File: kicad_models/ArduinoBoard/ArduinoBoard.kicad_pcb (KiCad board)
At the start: 2 copper layers, 90.5 x 70 mm, 21 parts, among them J1 5V Output, J2 Buttons, J3 PWM Output, J4 12V Input, J5 Conn_01x04_Pin, J6 Conn_01x04_Pin, J7 Conn_01x06_Pin, J8 Conn_01x06_Pin, J9 Position Input, SW1 SW_Push_Dual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

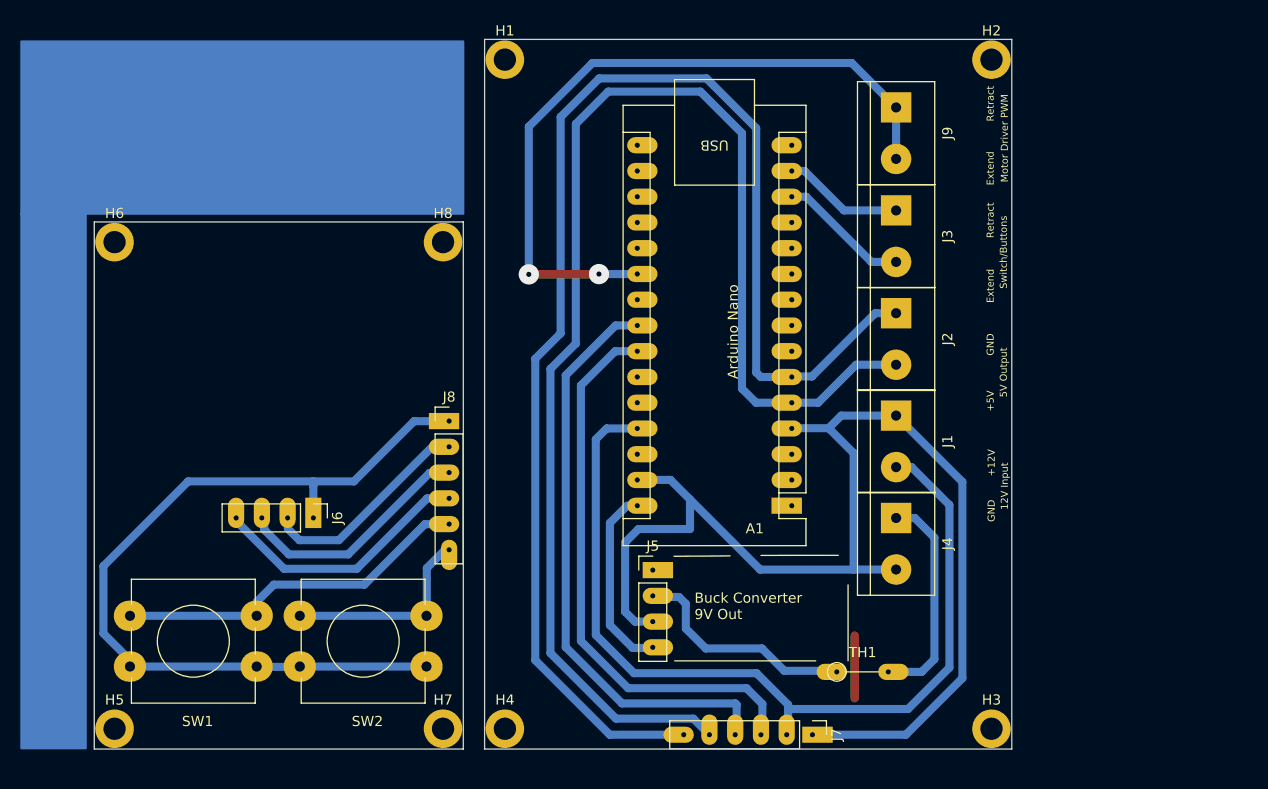
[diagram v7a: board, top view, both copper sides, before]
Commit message: Made some pretty significant changes to the PCB layout. Removed the need for a via path to cross over a couple of tracks.
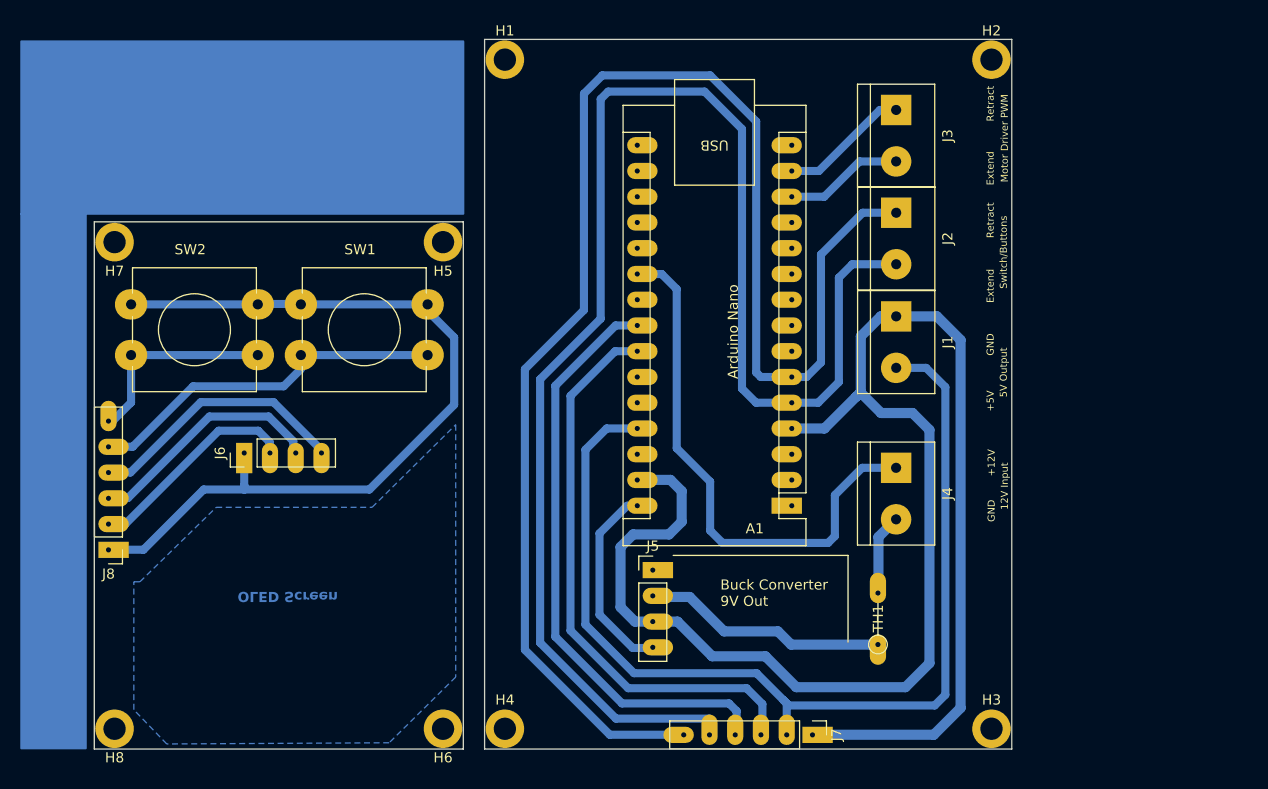
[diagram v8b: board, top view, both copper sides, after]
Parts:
- removed J9: Position Input, TerminalBlock:TerminalBlock_bornier-2_P5.08mm
- moved H5 57.9 mm to (84.4, 70.5), turned to 180 degrees
- moved H6 57.9 mm to (84.4, 118.5), turned to 180 degrees
- moved H7 57.9 mm to (52.0, 70.5), turned to 180 degrees
- moved H8 57.9 mm to (52.0, 118.5), turned to 180 degrees
- moved SW2 46.1 mm to (53.6, 76.6), turned to 0 degrees
- moved SW1 36.0 mm to (70.4, 76.6), turned to 0 degrees
- moved J8 35.9 mm to (51.4, 100.8), turned to 180 degrees
- moved J2 9.91 mm to (129.1, 67.6)
- moved J3 9.91 mm to (129.1, 57.5)
- moved J1 9.79 mm to (129.1, 77.8)
- moved J6 9.36 mm to (64.8, 91.3), turned to 90 degrees
- moved J4 4.95 mm to (129.1, 92.8)
- moved TH1 4.88 mm to (127.3, 110.2), turned to 90 degrees
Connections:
- net Net-(A1-VIN) renamed /VO+
- net Net-(J5-Pin_2) renamed /VI+
- net Net-(J6-Pin_1) renamed OLED_Board_GND
- net Net-(J6-Pin_2) renamed OLED_Board_5V
- net Net-(J8-Pin_6) renamed OLED_Board_Extend_Button
- A1 pad 29: Net-(J1-Pin_1) -> /GND
- A1 pad 4: Net-(J1-Pin_1) -> /GND
- J1 pad 1: Net-(J1-Pin_1) -> /GND
- J4 pad 1: Net-(J4-Pin_1) -> Net-(A1-A2)
- J4 pad 2: Net-(J1-Pin_1) -> Net-(J4-Pin_2)
- J5 pad 3: Net-(J1-Pin_1) -> /GND
- J7 pad 1: Net-(J1-Pin_1) -> /GND
- J8 pad 5: Net-(J8-Pin_5) -> OLED_Board_Retract_Button
- TH1 pad 2: Net-(J4-Pin_1) -> Net-(J4-Pin_2)
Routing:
- net /GND: track 0.00 -> 165.3 mm
- net Net-(J1-Pin_1): track 121.1 -> 0.00 mm
- net OLED_Board_Retract_Button: track 0.00 -> 22.7 mm
- net Net-(J8-Pin_5): track 35.2 -> 12.5 mm
- net Net-(J4-Pin_1): track 21.6 -> 0.00 mm
- net Net-(A1-A2): track 71.0 -> 54.0 mm, vias 2 -> 0
- net Net-(A1-+5V): track 88.7 -> 102.0 mm
- net Net-(A1-D2): track 134.2 -> 146.4 mm
- net Net-(A1-D3): track 136.0 -> 147.7 mm
- net Net-(J4-Pin_2): track 0.00 -> 8.01 mm
- net /VI+: track 29.8 -> 24.9 mm
- net Net-(A1-D10): track 13.0 -> 11.7 mm
- net OLED_Board_Extend_Button: track 19.1 -> 20.0 mm
- net Net-(A1-D11): track 11.9 -> 12.8 mm
- net /VO+: track 18.7 -> 19.5 mm
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- added copper zone on B.Cu, net (none)
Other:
- board text added: "Pos. Sensor"
- board text removed: "12V Power"
- board text removed: "Pos. Sensor (Use Either)"
